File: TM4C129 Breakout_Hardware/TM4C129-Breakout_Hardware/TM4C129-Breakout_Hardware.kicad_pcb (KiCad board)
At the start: 2 copper layers, 47 parts, among them J1 RJ45, J2 Conn_02x08, J3 Conn_02x08, J4 Conn_02x08, J5 Conn_02x02, J6 Conn_02x02, SW1 SW_Push, U1 HX1198FNL, U2 TM4C129ENCPDT, Y1 NX3225GA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

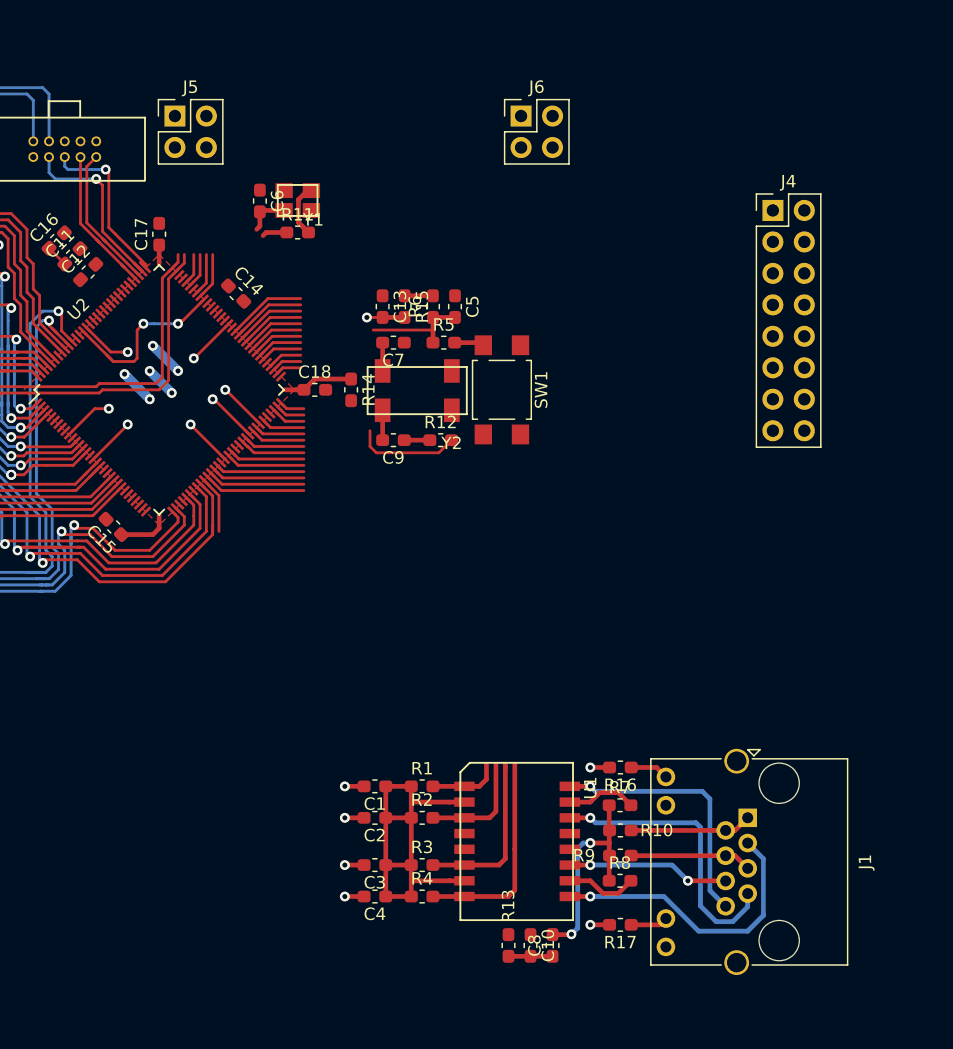
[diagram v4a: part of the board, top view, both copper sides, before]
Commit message: did ethernet circuitry
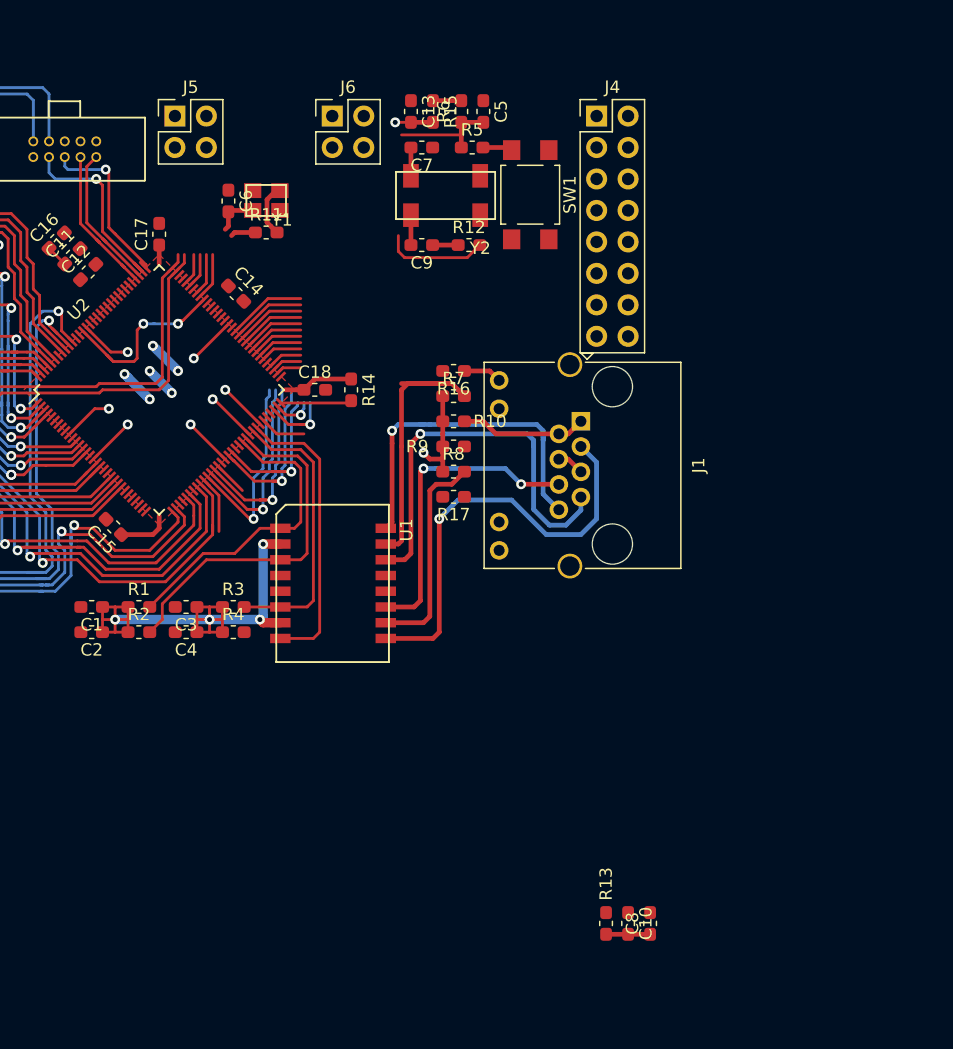
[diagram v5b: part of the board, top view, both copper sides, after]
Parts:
- moved R17 37.1 mm to (149.5, 61.2)
- moved R10 35.7 mm to (149.5, 55.1)
- moved R9 35.7 mm to (149.5, 57.1)
- moved R7 35.6 mm to (149.5, 53.1)
- moved R8 35.6 mm to (149.5, 59.2)
- moved R16 34.7 mm to (149.5, 51.1)
- moved J1 34.7 mm to (159.8, 55.1)
- moved C2 27.3 mm to (120.3, 72.1)
- moved R2 27.3 mm to (124.1, 72.1)
- moved C1 27.1 mm to (120.3, 70.1)
- moved R1 27.1 mm to (124.1, 70.1)
- moved R4 26.2 mm to (131.7, 72.1)
- moved C4 26.2 mm to (127.9, 72.1)
- moved R3 25.8 mm to (131.7, 70.1)
- moved C3 25.8 mm to (127.9, 70.1)
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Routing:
- net Net-(R7-Pad2): track 5.66 -> 24.1 mm
- net EN0RXI_P: track 14.1 -> 29.0 mm
- net EN0RXI_N: track 11.1 -> 25.0 mm
- net Net-(J1-Pad6): track 13.1 -> 25.2 mm
- net +3V3: track 56.6 -> 68.6 mm, vias 6 -> 10
- net Net-(R8-Pad2): track 5.77 -> 17.4 mm
- net Net-(J1-Pad3): track 23.7 -> 35.1 mm
- net Net-(J1-Pad7): track 23.1 -> 33.1 mm
- net Net-(C8-Pad2): track 17.5 -> 7.86 mm, vias 2 -> 1
- net GND: track 39.5 -> 30.2 mm, vias 13 -> 7
- net PWM3: track 7.51 -> 15.4 mm, vias 0 -> 1
- net PWM2: track 7.89 -> 15.8 mm, vias 0 -> 1
- net PWM1: track 8.26 -> 16.1 mm, vias 0 -> 1
- net Net-(J1-Pad4): track 9.83 -> 2.20 mm
- net Net-(J1-Pad8): track 20.9 -> 28.4 mm
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
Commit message: Finished layout and critical traces
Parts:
- moved C8 29.6 mm to (150.1, 70.2), turned to 270 degrees
- moved C10 28.0 mm to (151.9, 70.2), turned to 90 degrees
- moved R13 26.7 mm to (153.7, 70.2), turned to 90 degrees
- moved R12 21.5 mm to (139.7, 59.3), turned to 90 degrees
- moved R15 18.9 mm to (141.8, 48.0), turned to 180 degrees
- moved C7 18.8 mm to (145.7, 51.8)
- moved C5 17.8 mm to (146.6, 47.1), turned to 90 degrees
- moved R6 17.8 mm to (144.8, 47.1), turned to 270 degrees
- moved Y2 17.7 mm to (141.7, 53.1), turned to 270 degrees
- moved C13 16.7 mm to (141.8, 46.2), turned to 180 degrees
- moved C9 12.8 mm to (145.7, 53.6)
- moved R5 12.6 mm to (145.7, 44.5)
- moved SW1 9.45 mm to (153.2, 46.0), turned to 180 degrees
- moved J6 7.62 mm to (147.3, 30.5)
- moved R14 6.72 mm to (141.5, 59.3), turned to 90 degrees
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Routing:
- net T2_A: track 6.37 -> 50.9 mm
- net PWM1: track 16.1 -> 60.1 mm
- net T2_B: track 5.99 -> 48.3 mm
- net PWM2: track 15.8 -> 57.5 mm
- net T3_A: track 5.61 -> 45.4 mm
- net T3_B: track 5.24 -> 43.8 mm
- net PWM3: track 15.4 -> 54.0 mm
- net T5_B: track 3.73 -> 39.7 mm
- net PWM4: track 13.1 -> 49.0 mm
- net T4_A: track 4.86 -> 39.5 mm
- net PWM5: track 12.3 -> 46.2 mm
- net T5_A: track 4.11 -> 37.7 mm
- net T4_B: track 4.49 -> 38.0 mm
- net PWM6: track 3.29 -> 35.8 mm
- net PWM7: track 5.70 -> 36.8 mm
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
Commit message: finished layout
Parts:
- added G***: LOGO, MRDT_Silkscreens:0_MRDT_Logo_20mm, B.Cu at (126.5, 50.2)
- added G***: LOGO, MRDT_Silkscreens:z_sig_Andrew_Van_Horn_Sig_15mm, B.Cu at (152.4, 47.0)
- added REF**: 4_40_Hole, MRDT_Drill_Holes:4_40_Hole, F.Cu at (163.8, 71.1)
- moved R11 4.82 mm to (132.8, 35.3)
- moved C6 3.41 mm to (132.8, 40.4), turned to 180 degrees
- moved Y1 1.61 mm to (132.8, 37.8), turned to 180 degrees
- moved C13 1.52 mm to (140.3, 46.2)
- moved R15 1.52 mm to (140.3, 48.0)
- moved C14 1.12 mm to (132.8, 42.2), turned to 0 degrees
- moved C15 0.76 mm to (122.8, 63.9)
- moved C18 0.25 mm to (137.8, 52.3)
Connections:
- J5 pad 3: SCL0 -> SDA0
- J5 pad 4: SDA0 -> SCL0
- Y1 pad 1: /OSC0 -> Net-(R11-Pad2)
- Y1 pad 3: Net-(R11-Pad2) -> /OSC0
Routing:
- net +3V3: track 64.0 -> 135.6 mm
- net Net-(C11-Pad1): track 16.5 -> 28.1 mm
- net SCL0: track 2.85 -> 13.0 mm
- net SDA0: track 2.47 -> 11.5 mm
- net /OSC1: track 3.39 -> 12.1 mm
- net ~RST: track 3.08 -> 10.3 mm
- net /OSC0: track 5.77 -> 10.6 mm
- net GND: track 28.1 -> 30.4 mm, vias 7 -> 10
- net Net-(R11-Pad2): track 4.33 -> 2.12 mm
- net /VBAT: track 9.39 -> 7.62 mm
- net RX1: track 34.0 -> 32.7 mm
- net TX1: track 29.0 -> 27.8 mm
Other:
- board outline added: 63.5 x 47 mm
- board text added: "+3V3"
- board text added: "A"
- board text added: "GND"
- board text added: "I2C"
- board text added: "JTAG"
- board text added: "PWM"
- board text added: "Rx"
- board text added: "T"
- board text added: "TM4C129 Breakout Mars Rover Design Team Missouri S&T, 2020 Andrew Van Horn"
- board text added: "Tx"
